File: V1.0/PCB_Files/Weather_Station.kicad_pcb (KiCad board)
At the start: 2 copper layers, 36 parts, among them J1 N091-2832TSWFG02-H14, J2 USB_B_Micro, J3 Conn_01x04_Pin, U1 STM32F103C8T6, U2 HDC1080DMBR, U3 AMS1117-3.3, U5 SRV05-4

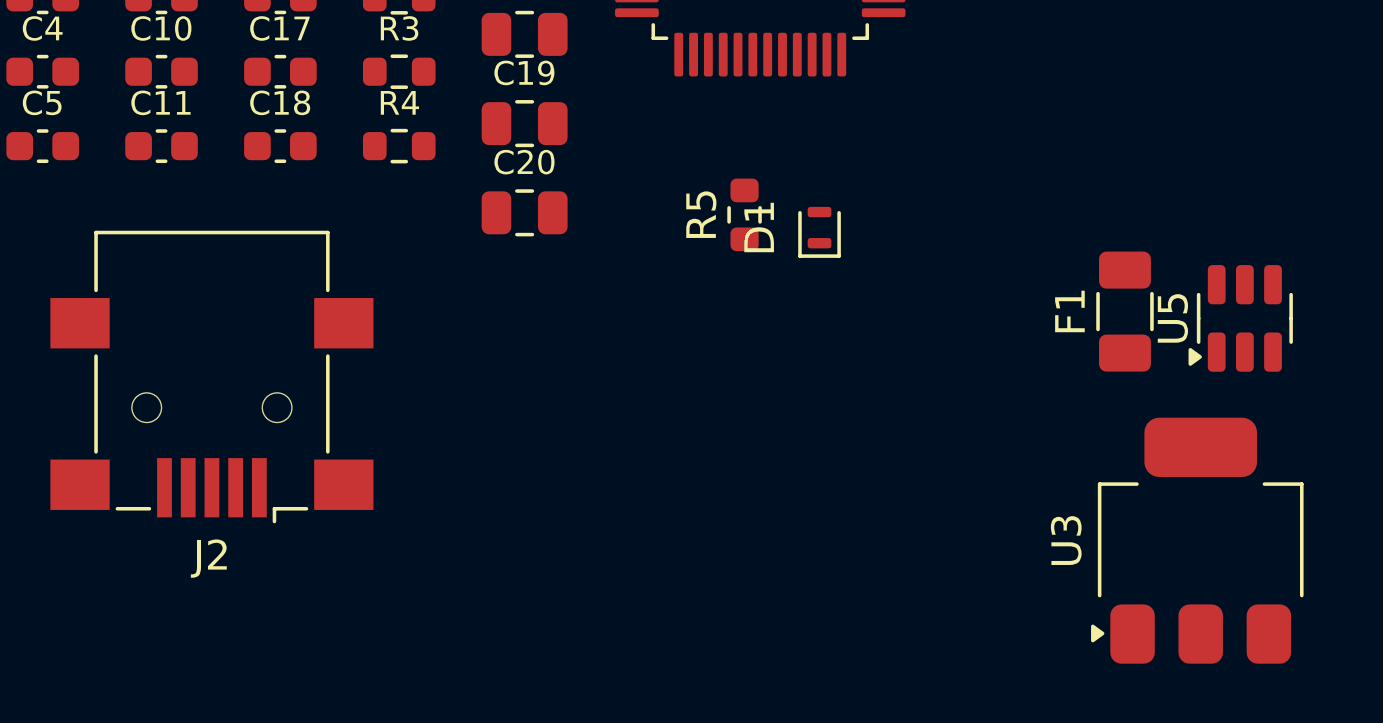
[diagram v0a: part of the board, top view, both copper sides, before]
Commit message: Updated Schematic with corrected TVS section.
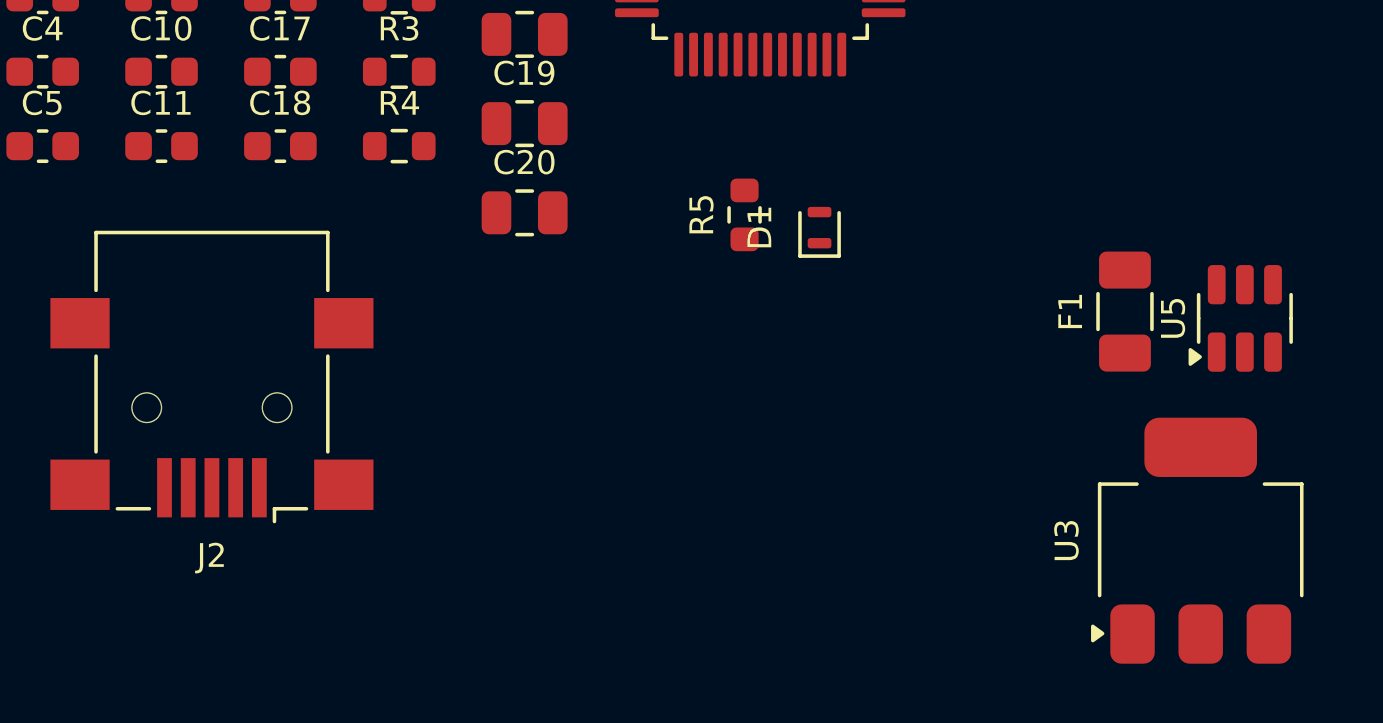
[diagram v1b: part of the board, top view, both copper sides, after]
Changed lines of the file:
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@@
 		(tags "CMS SOT")
 		(property "Reference" "U3"
-			(at 0 -4.500001 270)
+			(at 0 -4.500001 -90)
 			(layer "F.SilkS")
 			(effects
 				(font
-					(size 1 1)
+					(size 0.8 0.8)
 					(thickness 0.15)
 				)
@@
 		)
 		(property "Value" "AMS1117-3.3"
-			(at 0 4.500001 270)
+			(at 0 4.500001 -90)
 			(layer "F.Fab")
 			(effects
@@
 			(effects
 				(font
-					(size 1 1)
+					(size 0.8 0.8)
 					(thickness 0.15)
 				)
@@
 		(tags "QFN-2L Diode")
 		(property "Reference" "D1"
-			(at 0 -2.000001 270)
+			(at 0 -2.000001 -90)
 			(layer "F.SilkS")
 			(effects
 				(font
-					(size 1 1)
+					(size 0.8 0.8)
 					(thickness 0.15)
 				)
@@
 		)
 		(property "Value" "ESDA7P60-1U1M"
-			(at 0 2.000001 270)
+			(at 0 2.000001 -90)
 			(layer "F.Fab")
 			(effects
@@
 		)
 		(fp_text user "${REFERENCE}"
-			(at 0 -2.000001 270)
+			(at 0 -2.000001 -90)
 			(layer "F.Fab")
 			(effects
@@
 		(tags "fuse")
 		(property "Reference" "F1"
-			(at 0 -1.82 270)
+			(at 0 -1.82 -90)
 			(layer "F.SilkS")
 			(effects
 				(font
-					(size 1 1)
+					(size 0.8 0.8)
 					(thickness 0.15)
 				)
@@
 		)
 		(property "Value" "JFC1206-1100FS"
-			(at 0 1.82 270)
+			(at 0 1.82 -90)
 			(layer "F.Fab")
 			(effects
@@
 		)
 		(fp_text user "${REFERENCE}"
-			(at 0 0 270)
+			(at 0 0 -90)
 			(layer "F.Fab")
 			(effects
@@
 		(tags "SOT TO_SOT_SMD")
 		(property "Reference" "U5"
-			(at 0 -2.4 270)
+			(at 0 -2.4 -90)
 			(layer "F.SilkS")
 			(effects
 				(font
-					(size 1 1)
+					(size 0.8 0.8)
 					(thickness 0.15)
 				)
@@
 		)
 		(property "Value" "SRV05-4"
-			(at 0 2.4 270)
+			(at 0 2.4 -90)
 			(layer "F.Fab")
 			(effects
@@
 		)
 		(fp_text user "${REFERENCE}"
-			(at 0 0 270)
+			(at 0 0 -90)
 			(layer "F.Fab")
 			(effects
@@
 		(tags "resistor")
 		(property "Reference" "R5"
-			(at 0 -1.43 270)
+			(at 0 -1.43 -90)
 			(layer "F.SilkS")
 			(effects
 				(font
-					(size 1 1)
+					(size 0.8 0.8)
 					(thickness 0.15)
 				)
@@
 		)
 		(property "Value" "1k5"
-			(at 0 1.43 270)
+			(at 0 1.43 -90)
 			(layer "F.Fab")
 			(effects
@@
 		)
 		(fp_text user "${REFERENCE}"
-			(at 0 0 270)
+			(at 0 0 -90)
 			(layer "F.Fab")
 			(effects

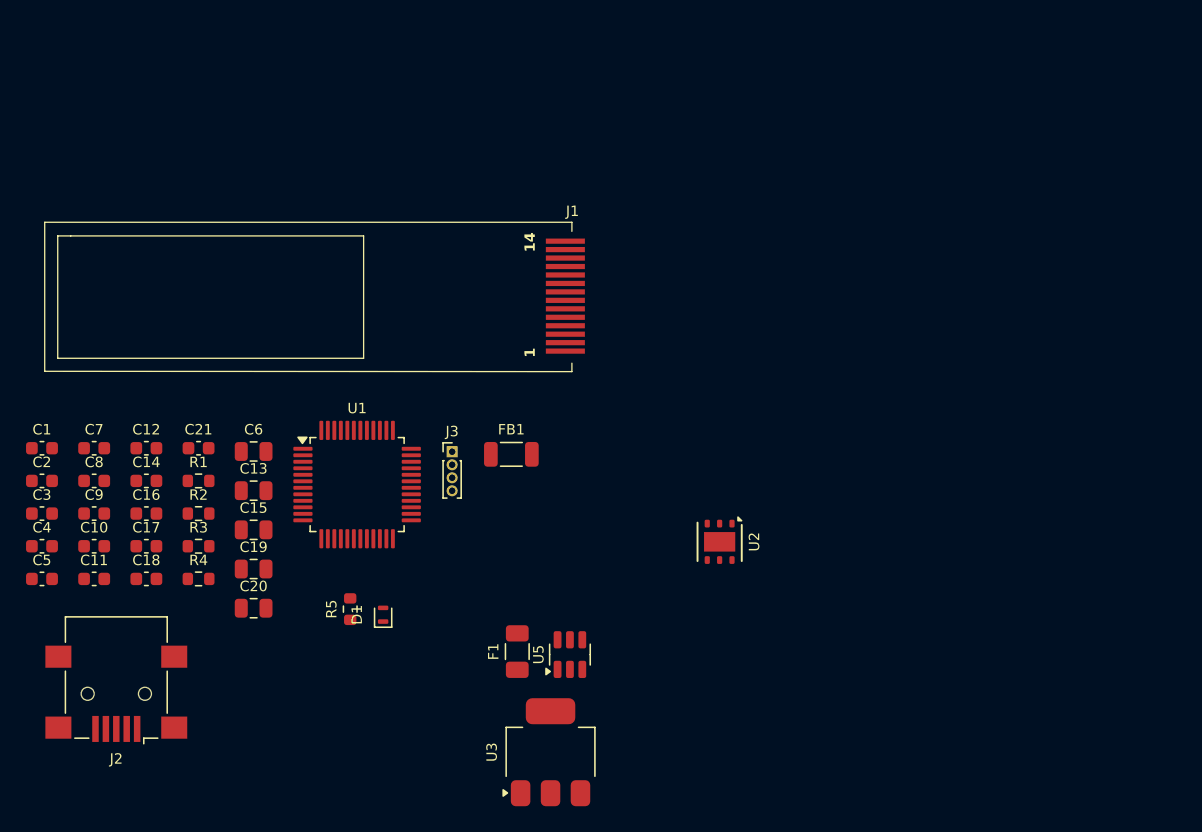
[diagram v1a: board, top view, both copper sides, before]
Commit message: Schematic should be 90% finished. Finishing touches and then design review.
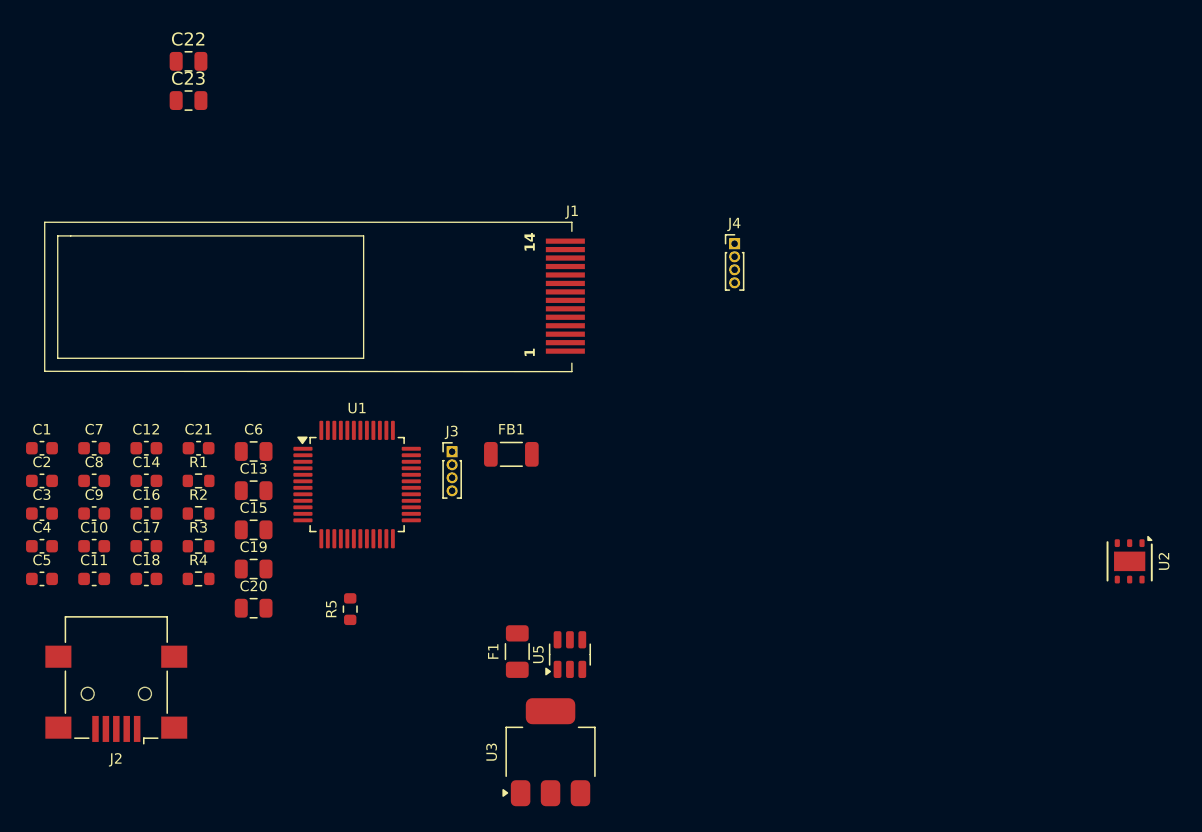
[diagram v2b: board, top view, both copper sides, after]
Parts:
- removed D1: ESDA7P60-1U1M, Diode_SMD:ST_QFN-2L_1.6x1.0mm
- added C22: 22u/10V, Capacitor_SMD:C_0805_2012Metric, F.Cu at (69.5, 29.0)
- added C23: 22u/10V, Capacitor_SMD:C_0805_2012Metric, F.Cu at (69.5, 32.0)
- added J4: Conn_01x04_Pin, Connector_PinHeader_1.00mm:PinHeader_1x04_P1.00mm_Vertical, F.Cu at (111.5, 43.0)
- moved U2 31.5 mm to (141.8, 67.4)
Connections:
- C1 pad 1: +3.3V -> unconnected-(C1-Pad1)
- C1 pad 2: GND -> unconnected-(C1-Pad2)
- C12 pad 1: GND -> unconnected-(C12-Pad1)
- C13 pad 1: +3.3V -> unconnected-(C13-Pad1)
- C13 pad 2: GND -> unconnected-(C13-Pad2)
- C14 pad 1: +3.3V -> unconnected-(C14-Pad1)
- C14 pad 2: GND -> unconnected-(C14-Pad2)
- C15 pad 2: GND -> unconnected-(C15-Pad2)
- C19 pad 1: +3.3V -> unconnected-(C19-Pad1)
- C19 pad 2: GND -> unconnected-(C19-Pad2)
- C2 pad 1: +3.3V -> unconnected-(C2-Pad1)
- C2 pad 2: GND -> unconnected-(C2-Pad2)
- C20 pad 1: +3.3V -> unconnected-(C20-Pad1)
- C20 pad 2: GND -> unconnected-(C20-Pad2)
- C21 pad 1: GND -> unconnected-(C21-Pad1)
- C21 pad 2: +3.3V -> unconnected-(C21-Pad2)
- C3 pad 1: +3.3V -> unconnected-(C3-Pad1)
- C3 pad 2: GND -> unconnected-(C3-Pad2)
- C4 pad 1: +3.3V -> unconnected-(C4-Pad1)
- C4 pad 2: GND -> unconnected-(C4-Pad2)
- C5 pad 1: +3.3V -> unconnected-(C5-Pad1)
- C5 pad 2: GND -> unconnected-(C5-Pad2)
- C6 pad 1: +3.3V -> unconnected-(C6-Pad1)
- C7 pad 1: +3.3VA -> unconnected-(C7-Pad1)
- C8 pad 1: +3.3VA -> unconnected-(C8-Pad1)
- C8 pad 2: GND -> unconnected-(C8-Pad2)
- FB1 pad 1: +3.3VA -> unconnected-(FB1-Pad1)
- FB1 pad 2: +3.3V -> unconnected-(FB1-Pad2)
- J1 pad 5: +3.3V -> unconnected-(J1-Pin_5-Pad5)
- J1 pad 8: +3.3V -> unconnected-(J1-Pin_8-Pad8)
- J1 pad 9: +3.3V -> unconnected-(J1-Pin_9-Pad9)
- J2 pad 2: /USB_DM_IN -> /USB_DM
- J2 pad 3: Net-(J2-D+) -> /USB_DP
- J2 pad 4: /USB_DP_IN -> unconnected-(J2-ID-Pad4)
- J2 pad 6: unconnected-(J2-Shield-Pad6) -> GND
- R3 pad 1: +3.3V -> unconnected-(R3-Pad1)
- R4 pad 2: GND -> unconnected-(R4-Pad2)
- R5 pad 2: Net-(J2-D+) -> /USB_DP
- U1 pad 24: +3.3V -> unconnected-(U1-VDD-Pad24)
- U1 pad 36: +3.3V -> unconnected-(U1-VDD-Pad36)
- U1 pad 48: +3.3V -> unconnected-(U1-VDD-Pad48)
- U1 pad 8: GND -> unconnected-(U1-VSSA-Pad8)
- U5 pad 1: /USB_DM -> /USB_DP
- U5 pad 3: /USB_DP -> /USB_DM
- U5 pad 4: /USB_DM_IN -> unconnected-(U5-IO3-Pad4)
- U5 pad 6: /USB_DP_IN -> unconnected-(U5-IO4-Pad6)

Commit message: Weird schematic error fixed.
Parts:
- moved U1 0.66 mm to (82.5, 62.2)
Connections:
- C1 pad 1: unconnected-(C1-Pad1) -> +3.3V
- C1 pad 2: unconnected-(C1-Pad2) -> GND
- C12 pad 1: unconnected-(C12-Pad1) -> GND
- C13 pad 1: unconnected-(C13-Pad1) -> +3.3V
- C13 pad 2: unconnected-(C13-Pad2) -> GND
- C14 pad 1: unconnected-(C14-Pad1) -> +3.3V
- C14 pad 2: unconnected-(C14-Pad2) -> GND
- C15 pad 2: unconnected-(C15-Pad2) -> GND
- C19 pad 1: unconnected-(C19-Pad1) -> +3.3V
- C19 pad 2: unconnected-(C19-Pad2) -> GND
- C2 pad 1: unconnected-(C2-Pad1) -> +3.3V
- C2 pad 2: unconnected-(C2-Pad2) -> GND
- C20 pad 1: unconnected-(C20-Pad1) -> +3.3V
- C20 pad 2: unconnected-(C20-Pad2) -> GND
- C21 pad 1: unconnected-(C21-Pad1) -> GND
- C21 pad 2: unconnected-(C21-Pad2) -> +3.3V
- C3 pad 1: unconnected-(C3-Pad1) -> +3.3V
- C3 pad 2: unconnected-(C3-Pad2) -> GND
- C4 pad 1: unconnected-(C4-Pad1) -> +3.3V
- C4 pad 2: unconnected-(C4-Pad2) -> GND
- C5 pad 1: unconnected-(C5-Pad1) -> +3.3V
- C5 pad 2: unconnected-(C5-Pad2) -> GND
- C6 pad 1: unconnected-(C6-Pad1) -> +3.3V
- C7 pad 1: unconnected-(C7-Pad1) -> +3.3VA
- C8 pad 1: unconnected-(C8-Pad1) -> +3.3VA
- C8 pad 2: unconnected-(C8-Pad2) -> GND
- FB1 pad 1: unconnected-(FB1-Pad1) -> +3.3VA
- FB1 pad 2: unconnected-(FB1-Pad2) -> +3.3V
- J1 pad 5: unconnected-(J1-Pin_5-Pad5) -> +3.3V
- J1 pad 8: unconnected-(J1-Pin_8-Pad8) -> +3.3V
- J1 pad 9: unconnected-(J1-Pin_9-Pad9) -> +3.3V
- R3 pad 1: unconnected-(R3-Pad1) -> +3.3V
- R4 pad 2: unconnected-(R4-Pad2) -> GND
- U1 pad 24: unconnected-(U1-VDD-Pad24) -> +3.3V
- U1 pad 36: unconnected-(U1-VDD-Pad36) -> +3.3V
- U1 pad 48: unconnected-(U1-VDD-Pad48) -> +3.3V
- U1 pad 8: unconnected-(U1-VSSA-Pad8) -> GND

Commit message: Started Layout of PCB.
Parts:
- removed C5: 100n/10V, Capacitor_SMD:C_0603_1608Metric
- added D1: KT-0603W, LED_SMD:LED_0603_1608Metric, F.Cu at (113.1, 24.9)
- added D2: KT-0603R, LED_SMD:LED_0603_1608Metric, F.Cu at (113.1, 27.5)
- added D3: 19-217/BHC-ZL1M2RY/6T, LED_SMD:LED_0603_1608Metric, F.Cu at (113.1, 30.1)
- added R6: 330R, Resistor_SMD:R_0603_1608Metric, F.Cu at (117.1, 24.9)
- added R7: 330R, Resistor_SMD:R_0603_1608Metric, F.Cu at (117.1, 27.4)
- added R8: 330R, Resistor_SMD:R_0603_1608Metric, F.Cu at (117.1, 29.9)
- added Y1: X322516MLB4SI, Crystal:Crystal_SMD_3225-4Pin_3.2x2.5mm, F.Cu at (216.2, 48.8)
- moved C4 176.6 mm to (233.8, 46.9), turned to -90 degrees
- moved C2 171.5 mm to (229.7, 56.1), turned to 180 degrees
- moved C3 167.6 mm to (224.6, 43.0)
- moved C1 162.7 mm to (220.5, 46.6), turned to 90 degrees
- moved C10 161.8 mm to (222.3, 42.2), turned to -90 degrees
- moved C7 158.4 mm to (220.5, 51.1), turned to 90 degrees
- moved C11 158.0 mm to (218.9, 47.5), turned to -90 degrees
- moved C8 157.6 mm to (219.8, 55.1), turned to 180 degrees
- moved C9 157.6 mm to (219.8, 58.3), turned to 180 degrees
- moved C6 155.1 mm to (229.6, 58.1), turned to 180 degrees
- moved C12 152.8 mm to (218.9, 50.5), turned to 90 degrees
- moved U1 145.2 mm to (227.2, 49.8)
- moved FB1 128.3 mm to (222.6, 56.7), turned to -90 degrees
- moved J1 4.48 mm to (95.2, 39.7)
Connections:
- U1 pad 10: unconnected-(U1-PA0-Pad10) -> /LED_B
- U1 pad 11: unconnected-(U1-PA1-Pad11) -> /LED_W
- U1 pad 12: unconnected-(U1-PA2-Pad12) -> /LED_R

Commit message: Made Progress with STM32 Layout.
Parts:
- moved C23 111.4 mm to (142.5, 116.2), turned to 90 degrees
- moved J2 105.6 mm to (160.2, 34.1)
- moved C22 103.7 mm to (136.4, 108.3)
- moved R3 98.0 mm to (168.3, 68.2), turned to -90 degrees
- moved R2 96.5 mm to (166.7, 68.2), turned to -90 degrees
- moved R1 95.1 mm to (165.1, 68.2), turned to -90 degrees
- moved F1 75.8 mm to (162.8, 40.8)
- moved C1 70.2 mm to (158.6, 79.8)
- moved C10 70.2 mm to (160.4, 75.3)
- moved C11 70.2 mm to (157.0, 80.7)
- moved C12 70.2 mm to (157.0, 83.7)
- moved C4 70.2 mm to (171.9, 80.0)
- moved C7 70.2 mm to (158.6, 84.2)
- moved C8 70.2 mm to (157.9, 88.2)
- moved C9 70.2 mm to (157.9, 91.5)
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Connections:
- net /USB_DM renamed /USB_D-
- net /USB_DP renamed /USB_D+
- C22 pad 2: Net-(C22-Pad2) -> GND
- C23 pad 2: Net-(C22-Pad2) -> GND
- F1 pad 2: Net-(J2-VBUS) -> /VBUS_IN
- J2 pad 1: Net-(J2-VBUS) -> /VBUS_IN
- R5 pad 1: Net-(J2-VBUS) -> VBUS
- U5 pad 5: Net-(J2-VBUS) -> VBUS

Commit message: Questions for Schwering now.
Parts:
- added J5: Conn_01x06_Pin, Connector_PinHeader_1.00mm:PinHeader_1x06_P1.00mm_Vertical, F.Cu at (103.4, 25.8)
- moved R5 92.0 mm to (173.5, 80.5), turned to -90 degrees
- moved J3 83.5 mm to (171.8, 74.9), turned to 90 degrees
- moved J4 75.5 mm to (179.9, 74.9), turned to -90 degrees
- moved J2 54.0 mm to (185.9, 81.5), turned to 90 degrees
- moved J1 49.9 mm to (138.2, 65.1)
- moved C22 49.4 mm to (182.2, 89.7), turned to -90 degrees
- moved U5 48.5 mm to (178.9, 81.9), turned to 0 degrees
- moved F1 47.3 mm to (178.8, 85.3), turned to 0 degrees
- moved U3 45.1 mm to (176.5, 91.0), turned to 180 degrees
- moved C23 37.8 mm to (174.3, 95.8), turned to 0 degrees
- moved U2 24.4 mm to (151.1, 90.0)
- moved C20 10.5 mm to (85.0, 70.0)
- moved R1 7.78 mm to (165.8, 76.0), turned to 0 degrees
- moved R2 7.14 mm to (168.2, 75.2)
- moved R3 7.13 mm to (169.7, 75.2)
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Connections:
- U5 pad 4: unconnected-(U5-IO3-Pad4) -> /USB_D-
- U5 pad 6: unconnected-(U5-IO4-Pad6) -> /USB_D+
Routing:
- net /USART1_TX: track 0.00 -> 17.4 mm, vias 0 -> 1
- net /USART1_RX: track 0.00 -> 16.4 mm, vias 0 -> 1
- net /USB_D+: track 0.00 -> 12.0 mm
- net /USB_D-: track 0.00 -> 12.0 mm
- net /SWDIO: track 0.00 -> 11.7 mm
- net /SWCLK: track 0.00 -> 11.6 mm
- net /I2C1_SCL: track 0.00 -> 9.83 mm
- net /I2C1_SDA: track 0.00 -> 8.83 mm
- net +3.3V: track 0.00 -> 7.93 mm
- net GND: track 0.00 -> 7.49 mm
- net /BOOT0: track 0.00 -> 3.74 mm
- net +3.3VA: track 0.00 -> 2.86 mm
- added copper zone on F.Cu, net +3.3V
- added copper zone on F.Cu, net /VBUS_IN
- added copper zone on F.Cu, net VBUS
